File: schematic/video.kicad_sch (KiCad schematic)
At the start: 12 parts, among them U10 MK4116P, U11 MK4116P, U12 MK4116P, U13 MK4116P, U14 MK4116P, U15 MK4116P, U16 MK4116P, U17 MK4116P, U9 TMS9928A

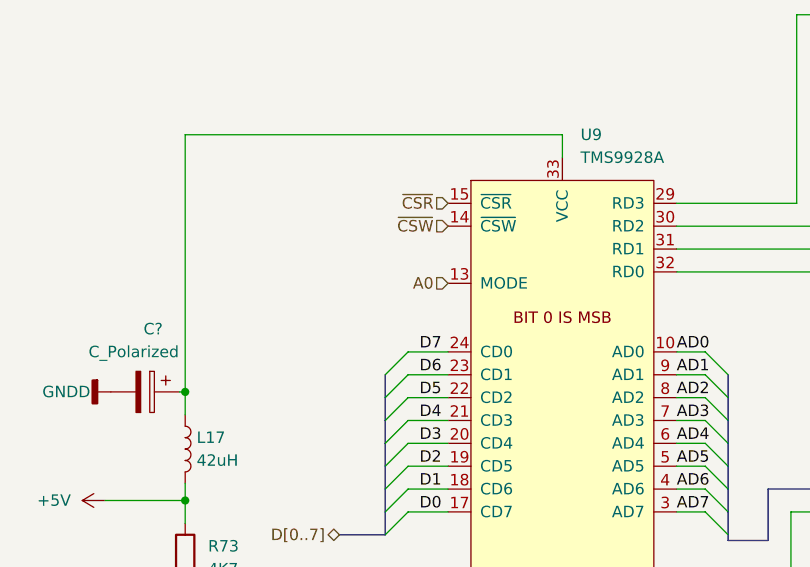
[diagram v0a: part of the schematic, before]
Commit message: fixed some more line names, added a expansion port io pin.
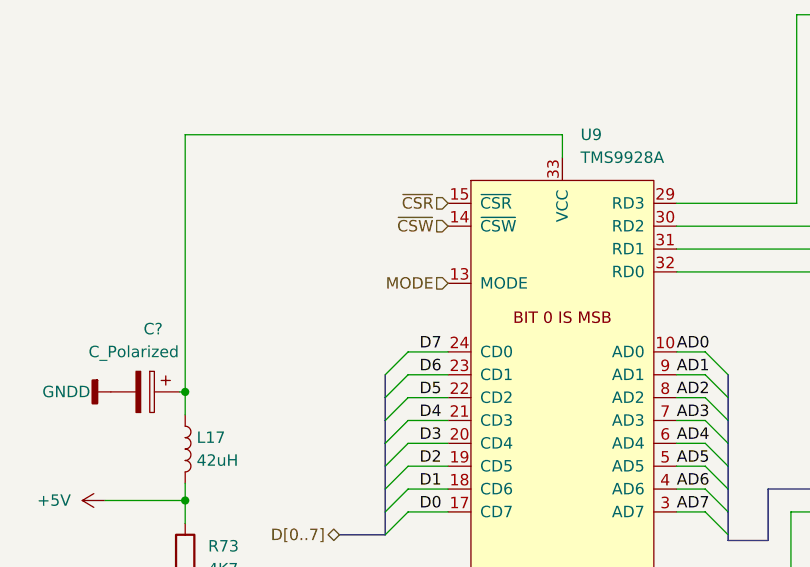
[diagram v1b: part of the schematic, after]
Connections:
- net A0 renamed MODE
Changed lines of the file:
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@@
     (effects (font (size 1.27 1.27)) (justify right))
   )
-  (hierarchical_label "A0" (shape input) (at 63.5 57.15 180)
+  (hierarchical_label "MODE" (shape input) (at 63.5 57.15 180)
     (effects (font (size 1.27 1.27)) (justify right))
   )

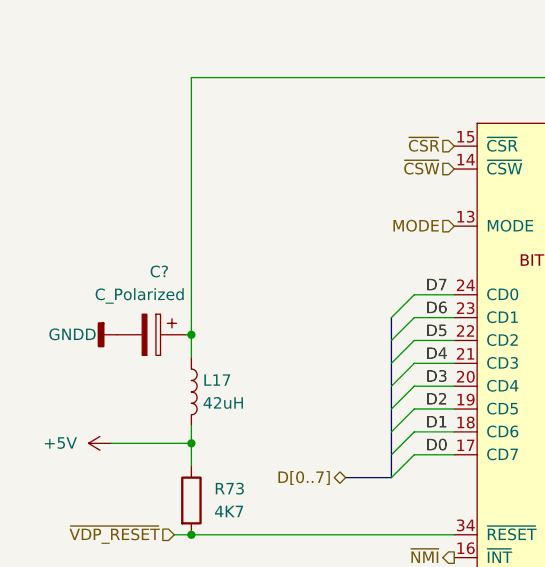
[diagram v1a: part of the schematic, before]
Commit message: power supply added, controller circuit added. Controller is a very odd duck to say the least. Seems they wanted to have plenty of current, maybe due to the steering wheel attachement?
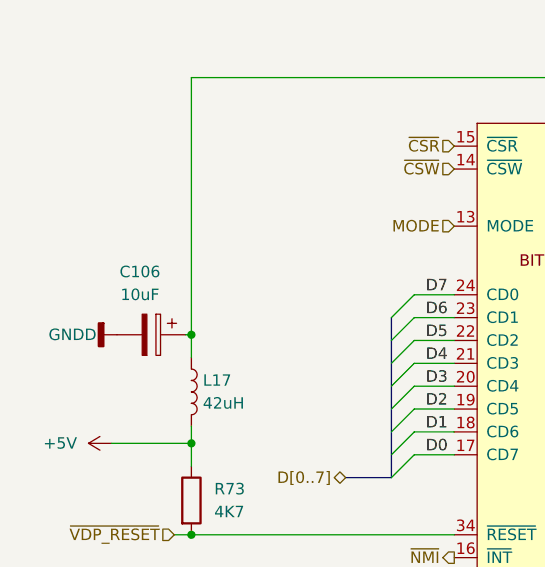
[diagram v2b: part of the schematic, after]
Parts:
- C106: renamed from C?; value C_Polarized -> 10uF

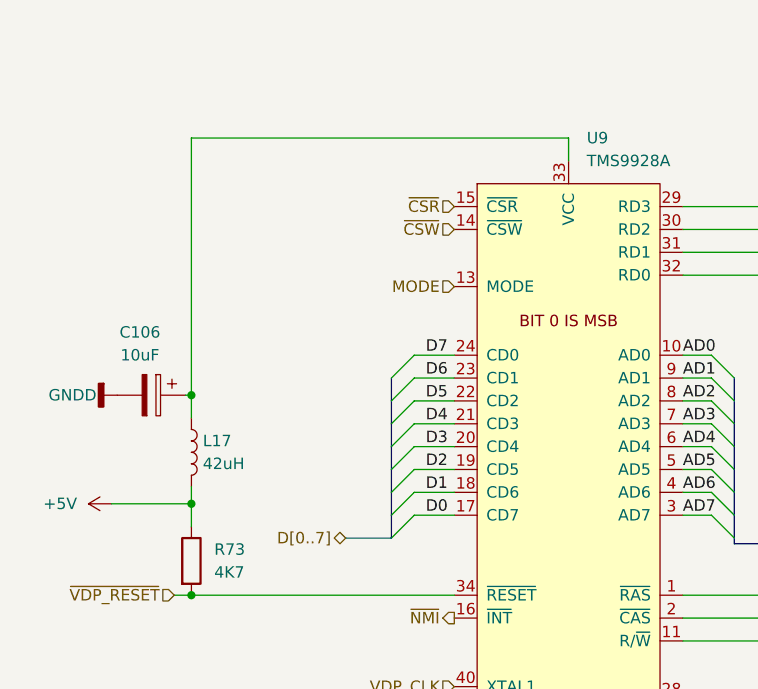
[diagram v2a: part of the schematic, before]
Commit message: first version of clock-reset circuits. Its a bit complicated and will need some revisions.
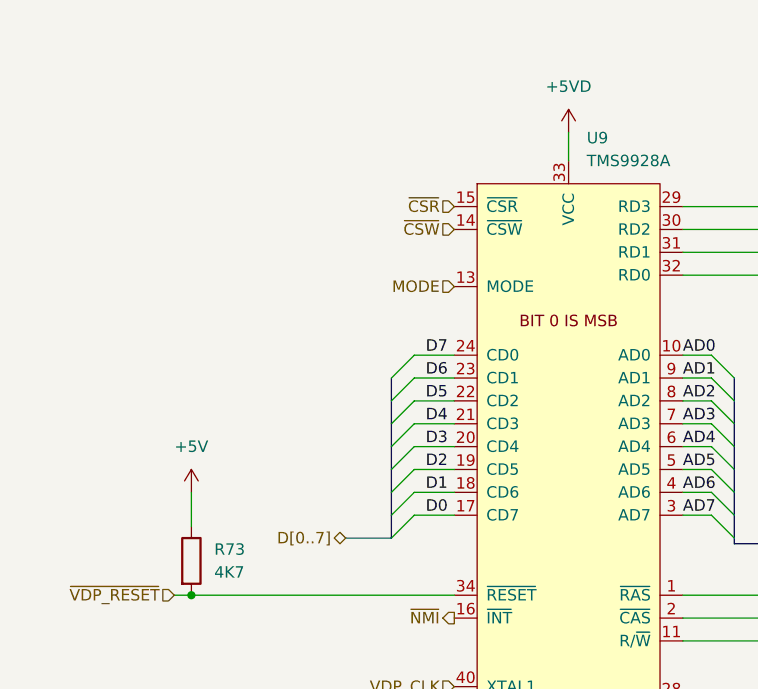
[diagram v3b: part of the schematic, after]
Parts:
- removed C106: 10uF, symbol Device:C_Polarized
- removed L17: 42uH, symbol Device:L
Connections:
- net +5VD: now reaches U9.33 (VCC)
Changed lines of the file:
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@@
   (junction (at 112.395 82.55) (diameter 0) (color 0 0 0 0)
   )
-  (junction (at 34.29 69.215) (diameter 0) (color 0 0 0 0)
-  )
   (junction (at 174.625 87.63) (diameter 0) (color 0 0 0 0)
-  )
-  (junction (at 34.29 81.28) (diameter 0) (color 0 0 0 0)
   )
   (junction (at 175.895 82.55) (diameter 0) (color 0 0 0 0)
@@
     (stroke (width 0) (type default) (color 0 0 0 0))
   )
-  (wire (pts (xy 34.29 81.28) (xy 34.29 83.82))
+  (wire (pts (xy 34.29 80.01) (xy 34.29 83.82))
     (stroke (width 0) (type default) (color 0 0 0 0))
   )
@@
     (stroke (width 0) (type default) (color 0 0 0 0))
   )
-  (wire (pts (xy 76.2 40.64) (xy 76.2 43.18))
+  (wire (pts (xy 76.2 40.005) (xy 76.2 43.18))
     (stroke (width 0) (type default) (color 0 0 0 0))
   )
@@
     (stroke (width 0) (type default) (color 0 0 0 0))
   )
-  (wire (pts (xy 34.29 69.215) (xy 34.29 40.64))
-    (stroke (width 0) (type default) (color 0 0 0 0))
-  )
   (wire (pts (xy 104.14 85.09) (xy 104.14 93.98))
     (stroke (width 0) (type default) (color 0 0 0 0))
@@
     (stroke (width 0) (type default) (color 0 0 0 0))
   )
-  (wire (pts (xy 34.29 69.215) (xy 33.655 69.215))
-    (stroke (width 0) (type default) (color 0 0 0 0))
-  )
   (wire (pts (xy 107.315 135.255) (xy 173.355 135.255))
     (stroke (width 0) (type default) (color 0 0 0 0))
@@
     (stroke (width 0) (type default) (color 0 0 0 0))
   )
-  (wire (pts (xy 34.29 40.64) (xy 76.2 40.64))
-    (stroke (width 0) (type default) (color 0 0 0 0))
-  )
   (wire (pts (xy 142.875 87.63) (xy 174.625 87.63))
     (stroke (width 0) (type default) (color 0 0 0 0))
@@
     (stroke (width 0) (type default) (color 0 0 0 0))
   )
-  (wire (pts (xy 34.29 79.375) (xy 34.29 81.28))
-    (stroke (width 0) (type default) (color 0 0 0 0))
-  )
   (bus (pts (xy 172.085 71.755) (xy 172.085 80.01))
     (stroke (width 0) (type default) (color 0 0 0 0))
@@
     (stroke (width 0) (type default) (color 0 0 0 0))
   )
-  (wire (pts (xy 25.4 81.28) (xy 34.29 81.28))
-    (stroke (width 0) (type default) (color 0 0 0 0))
-  )
   (wire (pts (xy 178.435 109.22) (xy 174.625 109.22))
     (stroke (width 0) (type default) (color 0 0 0 0))
@@
   )
   (bus (pts (xy 172.085 80.01) (xy 203.835 80.01))
-    (stroke (width 0) (type default) (color 0 0 0 0))
-  )
-  (wire (pts (xy 34.29 71.755) (xy 34.29 69.215))
     (stroke (width 0) (type default) (color 0 0 0 0))
   )
@@
     )
     (pin "1")
-  )
-  (symbol (lib_id "Device:L") (at 34.29 75.565 0) (unit 1)
-    (in_bom yes) (on_board yes) (fields_autoplaced)
-    (property "Reference" "L17" (id 0) (at 35.56 74.2949 0)
-      (effects (font (size 1.27 1.27)) (justify left))
-    )
-    (property "Value" "42uH" (id 1) (at 35.56 76.8349 0)
-      (effects (font (size 1.27 1.27)) (justify left))
-    )
-    (property "Footprint" "" (id 2) (at 34.29 75.565 0)
-      (effects (font (size 1.27 1.27)) hide)
-    )
-    (property "Datasheet" "~" (id 3) (at 34.29 75.565 0)
-      (effects (font (size 1.27 1.27)) hide)
-    )
-    (pin "1")
-    (pin "2")
   )
   (symbol (lib_id "power:-5V") (at 217.805 41.275 0) (unit 1)
@@
     (pin "1")
   )
+  (symbol (lib_id "power:+5VD") (at 76.2 40.005 0) (unit 1)
+    (in_bom yes) (on_board yes) (fields_autoplaced)
+    (property "Reference" "#PWR?" (id 0) (at 76.2 43.815 0)
+      (effects (font (size 1.27 1.27)) hide)
+    )
+    (property "Value" "+5VD" (id 1) (at 76.2 34.925 0))
+    (property "Footprint" "" (id 2) (at 76.2 40.005 0)
+      (effects (font (size 1.27 1.27)) hide)
+    )
+    (property "Datasheet" "" (id 3) (at 76.2 40.005 0)
+      (effects (font (size 1.27 1.27)) hide)
+    )
+    (pin "1")
+  )
   (symbol (lib_id "power:-5V") (at 186.055 41.275 0) (unit 1)
     (in_bom yes) (on_board yes) (fields_autoplaced)
@@
     (pin "1")
   )
-  (symbol (lib_id "power:+5V") (at 25.4 81.28 90) (unit 1)
+  (symbol (lib_id "power:+5V") (at 34.29 80.01 0) (unit 1)
     (in_bom yes) (on_board yes) (fields_autoplaced)
-    (property "Reference" "#PWR?" (id 0) (at 29.21 81.28 0)
-      (effects (font (size 1.27 1.27)) hide)
-    )
-    (property "Value" "+5V" (id 1) (at 21.59 81.2799 90)
-      (effects (font (size 1.27 1.27)) (justify left))
-    )
-    (property "Footprint" "" (id 2) (at 25.4 81.28 0)
-      (effects (font (size 1.27 1.27)) hide)
-    )
-    (property "Datasheet" "" (id 3) (at 25.4 81.28 0)
+    (property "Reference" "#PWR?" (id 0) (at 34.29 83.82 0)
+      (effects (font (size 1.27 1.27)) hide)
+    )
+    (property "Value" "+5V" (id 1) (at 34.29 74.93 0))
+    (property "Footprint" "" (id 2) (at 34.29 80.01 0)
+      (effects (font (size 1.27 1.27)) hide)
+    )
+    (property "Datasheet" "" (id 3) (at 34.29 80.01 0)
       (effects (font (size 1.27 1.27)) hide)
     )
@@
     (pin "1")
   )
-  (symbol (lib_id "power:GNDD") (at 26.035 69.215 270) (unit 1)
-    (in_bom yes) (on_board yes)
-    (property "Reference" "#PWR?" (id 0) (at 19.685 69.215 0)
-      (effects (font (size 1.27 1.27)) hide)
-    )
-    (property "Value" "GNDD" (id 1) (at 18.415 69.215 90)
-      (effects (font (size 1.27 1.27)) (justify left))
-    )
-    (property "Footprint" "" (id 2) (at 26.035 69.215 0)
-      (effects (font (size 1.27 1.27)) hide)
-    )
-    (property "Datasheet" "" (id 3) (at 26.035 69.215 0)
-      (effects (font (size 1.27 1.27)) hide)
-    )
-    (pin "1")
-  )
-  (symbol (lib_id "Device:C_Polarized") (at 29.845 69.215 270) (unit 1)
-    (in_bom yes) (on_board yes)
-    (property "Reference" "C106" (id 0) (at 28.575 62.23 90))
-    (property "Value" "10uF" (id 1) (at 28.575 64.77 90))
-    (property "Footprint" "" (id 2) (at 26.035 70.1802 0)
-      (effects (font (size 1.27 1.27)) hide)
-    )
-    (property "Datasheet" "~" (id 3) (at 29.845 69.215 0)
-      (effects (font (size 1.27 1.27)) hide)
-    )
-    (pin "1")
-    (pin "2")
-  )
   (symbol (lib_id "power:+12V") (at 151.765 93.98 0) (unit 1)

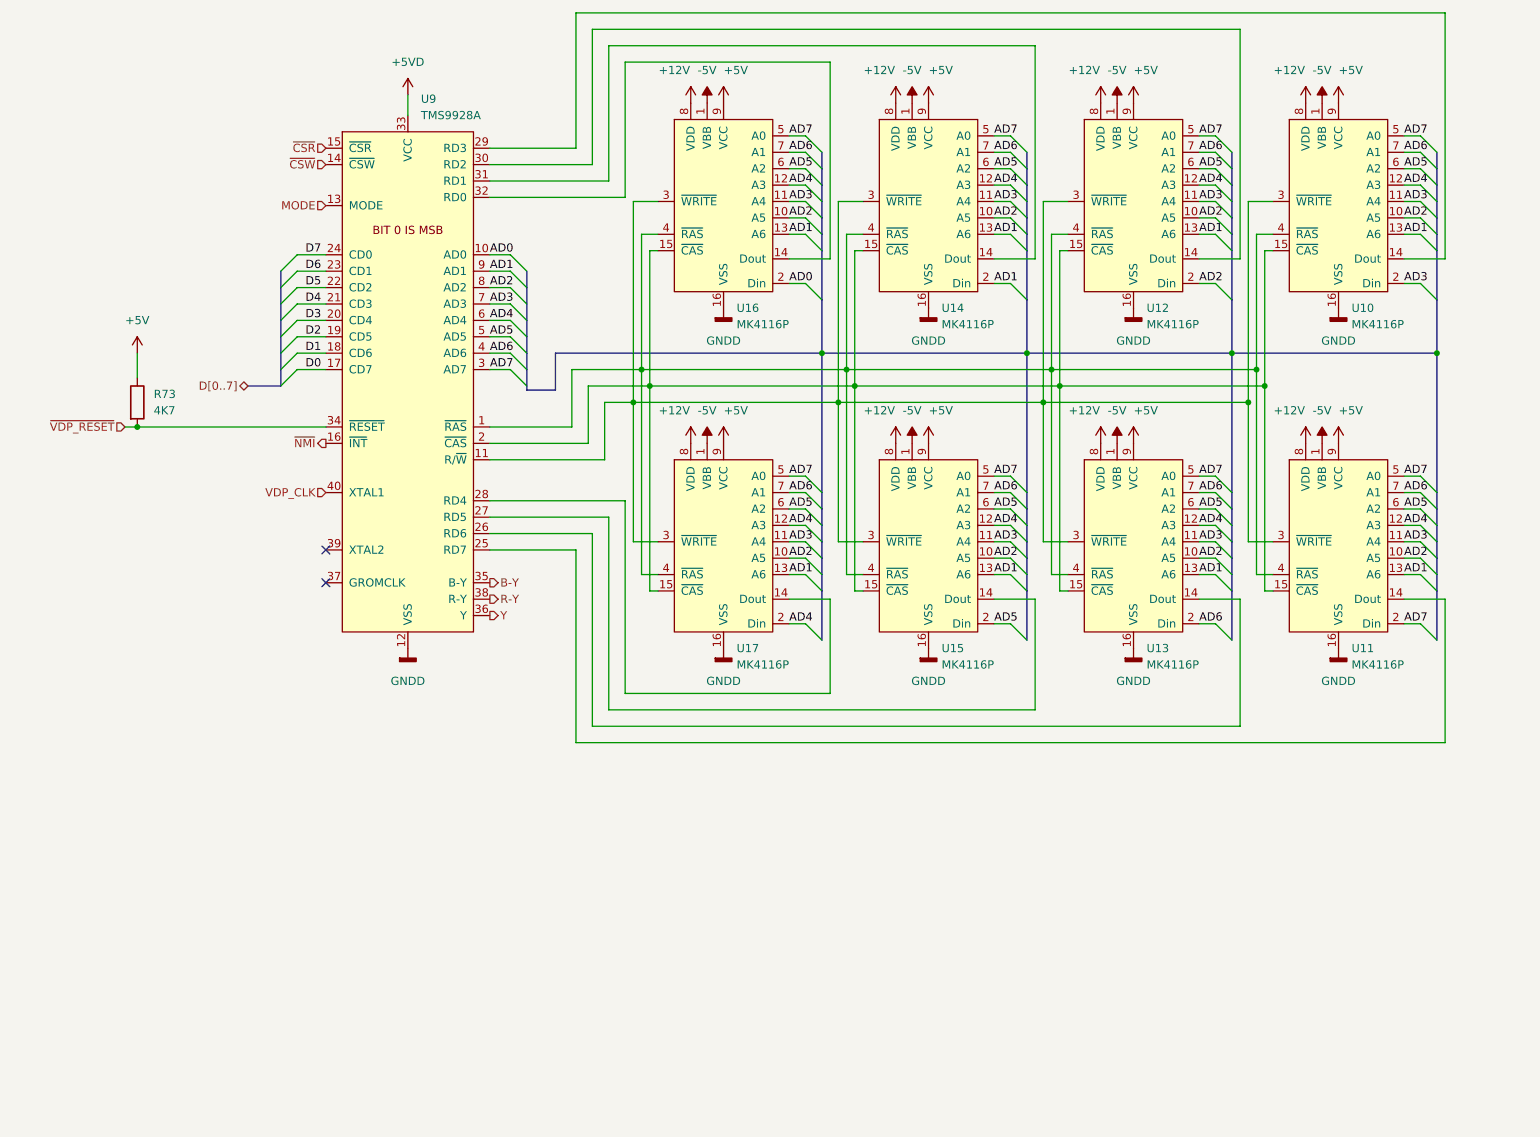
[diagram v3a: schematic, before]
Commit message: altered and did some cleanup of the way the wires were run. Finished expansion port routes to rf modulator. Added ext_psu for future external power supply design (will be an off the shelf psu block).
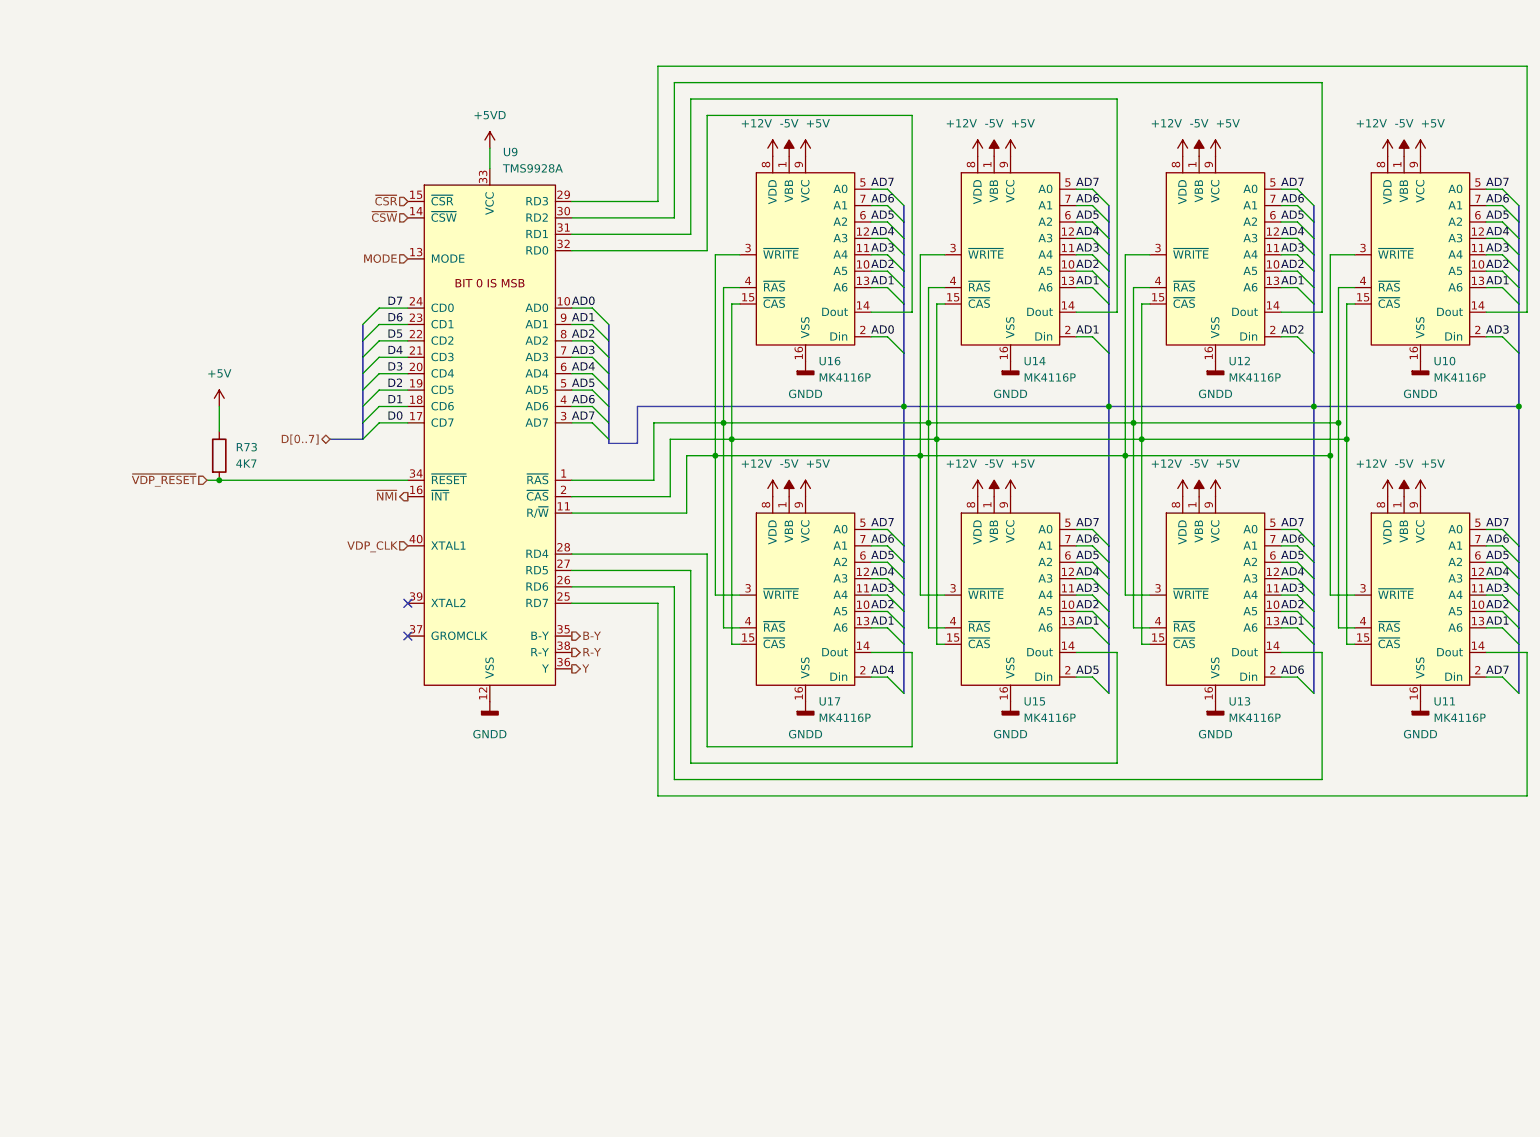
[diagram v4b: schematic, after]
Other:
- moved on the sheet: R73, U10, U11, U12, U13, U14, U15, U16, U17, U9
